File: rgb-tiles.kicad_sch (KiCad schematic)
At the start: 0 parts

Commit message: draw first rgb tile schematic
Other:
- added sheet controller (schematic/controller.kicad_sch)
- added sheet interfaces (schematic/interfaces.kicad_sch)
- added sheet leds (schematic/leds.kicad_sch)
- added sheet power (schematic/power.kicad_sch)
- added sheet usb-led-data (schematic/usb-led-data.kicad_sch)
- note added: "RGB TILES"
- title: (none) -> RGB Tiles
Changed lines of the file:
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@@
-(kicad_sch
-	(version 20260306)
-	(generator "eeschema")
-	(generator_version "10.0")
-	(paper "A4")
-	(sheet_instances
-		(path "/"
-			(page "1")
-		)
-	)
-	(embedded_fonts no)
-)

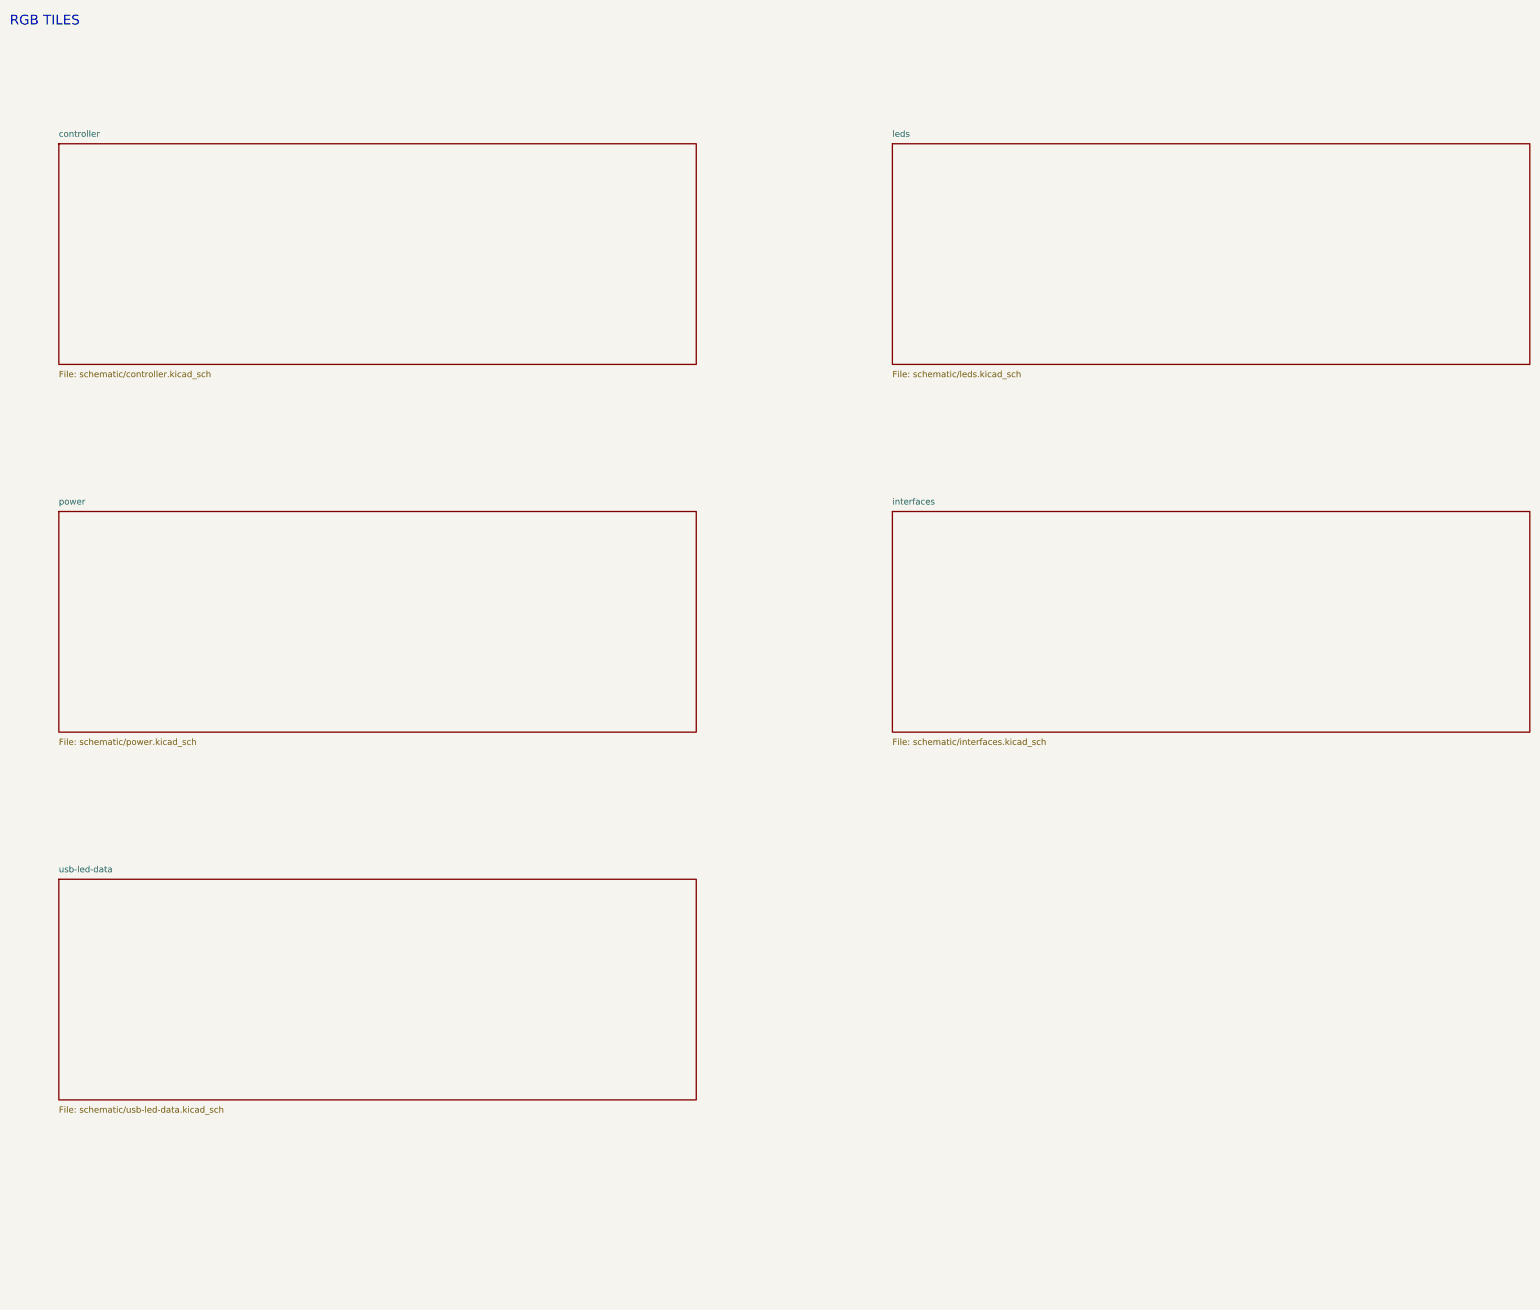
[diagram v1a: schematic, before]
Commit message: finish tile schematics and connector footprints
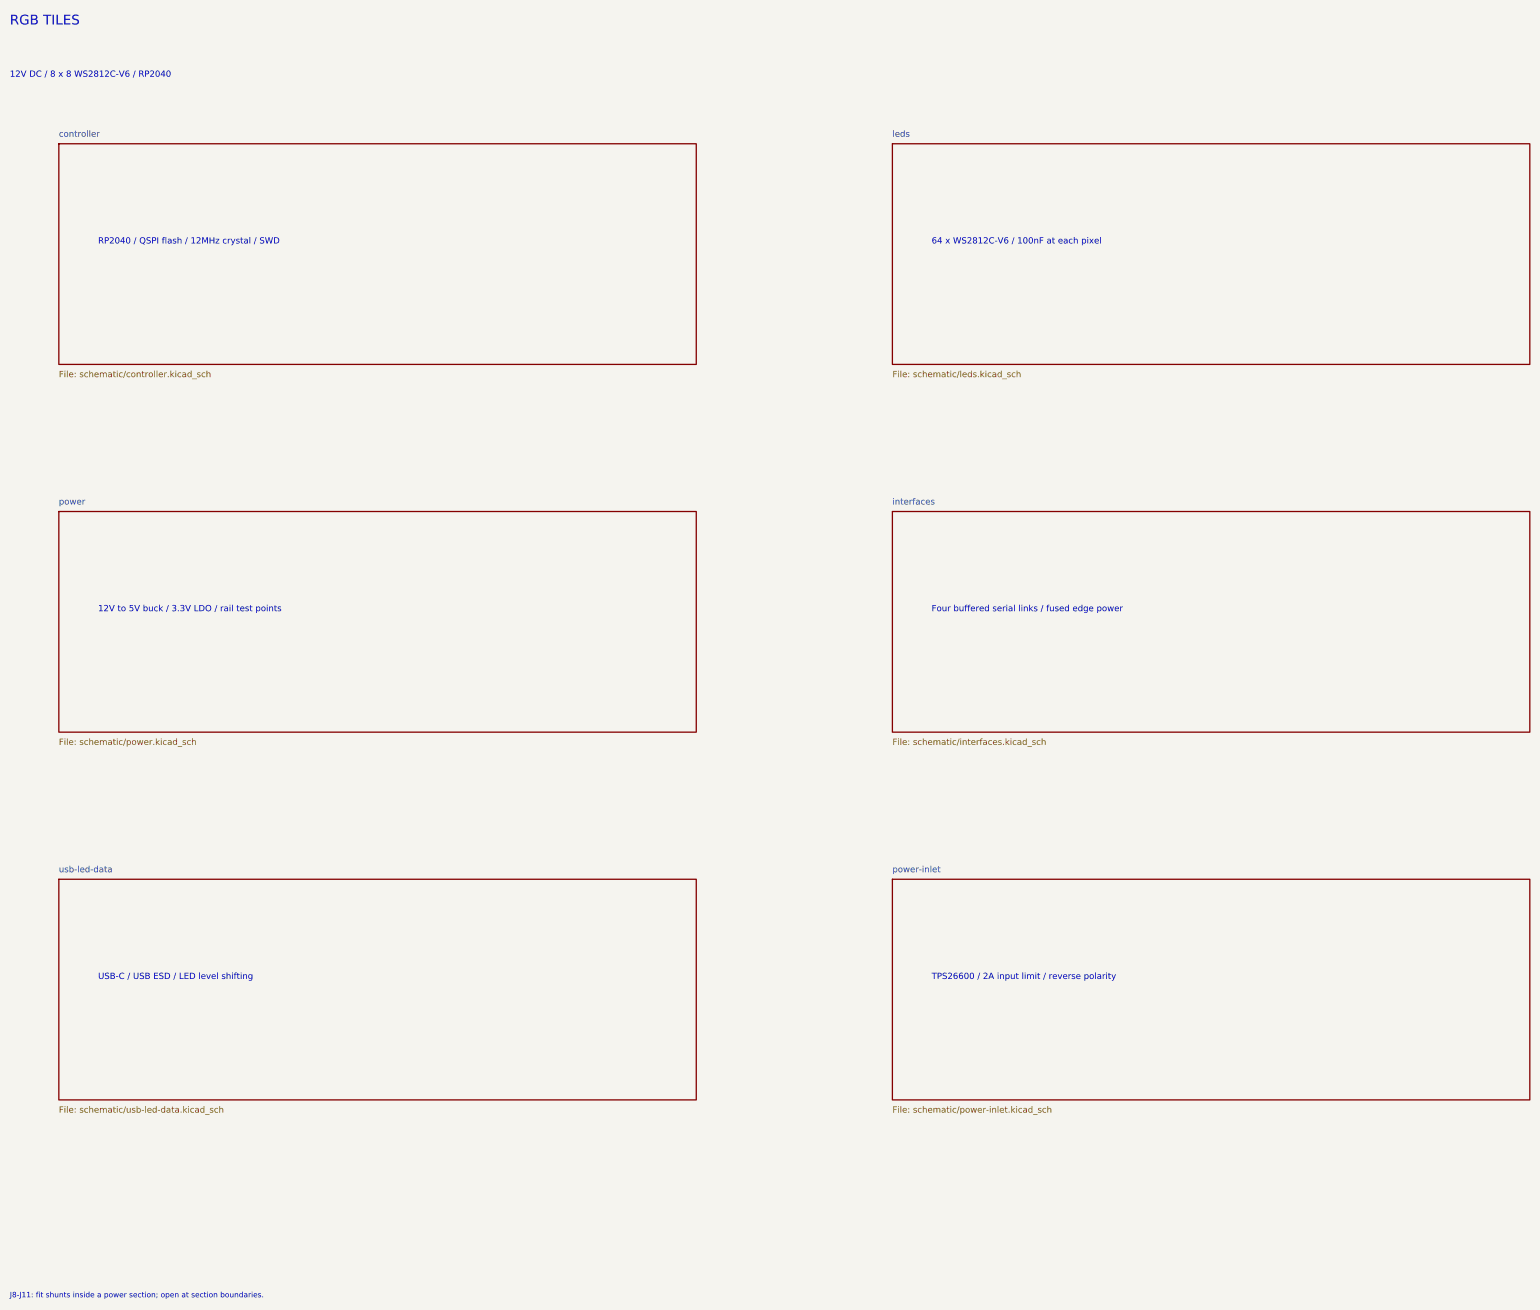
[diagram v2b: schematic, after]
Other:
- added sheet power-inlet (schematic/power-inlet.kicad_sch)
- note added: "12V DC / 8 x 8 WS2812C-V6 / RP2040"
- note added: "12V to 5V buck / 3.3V LDO / rail test points"
- note added: "64 x WS2812C-V6 / 100nF at each pixel"
- note added: "Four buffered serial links / fused edge power"
- note added: "J8-J11: fit shunts inside a power section; open at section boundaries."
- note added: "RP2040 / QSPI flash / 12MHz crystal / SWD"
- note added: "TPS26600 / 2A input limit / reverse polarity"
- note added: "USB-C / USB ESD / LED level shifting"
